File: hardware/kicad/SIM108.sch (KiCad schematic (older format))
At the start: 56 parts, among them J1 Screw_Terminal_01x09, J2 CAN, SW1 PRG, SW2 INSTANCE, SW3 BUS, U1 MCP2551-I-P, U2 TMR_2411, U3 74HCT595, U4 74HCT595, U5 Teensy_4.0

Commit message: Relay PCB
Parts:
- removed C1, C2, C3, C4: 100nF, Capacitor_SMD:C_0805_2012Metric, symbol Device:CP_Small
- removed C5: 100nF, Capacitor_THT:CP_Radial_D5.0mm_P2.50mm, symbol Device:CP_Small
- removed D1, D18, D19, D2, D20, D21, D22, D23, D24, D25, D3, D4, D5, D6, D7, D8, D9: LED, LED_THT:LED_D1.8mm_W3.3mm_H2.4mm, symbol Device:LED
- removed F1: 1A, Fuse:Fuse_Littelfuse_395Series, symbol Device:Polyfuse
- removed J2: CAN, Connector_PinHeader_2.54mm:PinHeader_1x05_P2.54mm_Vertical, symbol Connector:Screw_Terminal_01x05
- removed R1: 4K7 0.125W, Resistor_SMD:R_0805_2012Metric, symbol Device:R
- removed R2: 120R 0.5W, Resistor_THT:R_Axial_DIN0207_L6.3mm_D2.5mm_P7.62mm_Horizontal, symbol Device:R
- removed R28, R29, R3, R30, R31, R32, R33, R34, R35, R40, R41, R42, R43, R44, R45, R46, R47: 560R, Resistor_SMD:R_0805_2012Metric, symbol Device:R
- removed R36, R38: 2K2 0.125W, Resistor_SMD:R_0805_2012Metric, symbol Device:R
- removed R37, R39: 3K3 0.125W, Resistor_SMD:R_0805_2012Metric, symbol Device:R
- removed SW1: PRG, Button_Switch_THT:SW_TH_Tactile_Omron_B3F-10xx, symbol Switch:SW_MEC_5E
- removed SW2: INSTANCE, Package_DIP:DIP-16_W7.62mm, symbol Switch:SW_DIP_x08
- removed SW3: BUS, Package_DIP:DIP-4_W7.62mm_LongPads, symbol Switch:SW_DIP_x02
- removed U1: MCP2551-I-P, Package_SO:SOIC-8_3.9x4.9mm_P1.27mm, symbol Interface_CAN_LIN:MCP2551-I-P
- removed U2: TMR_2411, PDJR_DC-DC_Converters:TMR_2411, symbol SIM108-rescue:TMR_2411-pdjr
- removed U3, U4: 74HCT595, Package_SO:SO-16_3.9x9.9mm_P1.27mm, symbol 74xx:74HC595
- removed U5: Teensy_4.0, Package_DIP:DIP-28_W15.24mm_LongPads, symbol SIM108-rescue:Teensy_3.2-pdjr
- added D101, D102, D103, D104, D105, D106, D107, D108: IN4007, Diode_SMD:D_SOT-23_ANK, symbol Simulation_SPICE:DIODE
- added Q101, Q103, Q105, Q107, Q109, Q111, Q113, Q115: BC547, Package_TO_SOT_SMD:TSOT-23, symbol Transistor_BJT:BC547
- added Q102, Q104, Q106, Q108, Q110, Q112, Q114, Q116: BC337-40, Package_TO_SOT_SMD:TSOT-23, symbol Transistor_BJT:BC337
- added R101, R104, R107, R110, R113, R116, R119, R122: 4K7 0.125W, Resistor_SMD:R_0805_2012Metric, symbol Device:R
- added R102, R105, R108, R111, R114, R117, R120, R123: 10K 0.5W, Resistor_SMD:R_0805_2012Metric, symbol Device:R
- added R103, R106, R109, R112, R115, R118, R121, R124: 100R 0.25W, Resistor_SMD:R_0805_2012Metric, symbol Device:R
- added U101, U102, U103, U104, U105, U106, U107, U108: SFH617A-1, Package_DIP:SMDIP-4_W7.62mm, symbol Isolator:SFH617A-1
- renumbered J1 to J101
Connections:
- net labels added: +3.3V, D16, D17, D18, D19, D20, D21, D22, D23
- net labels removed: +5V, 3V3, ADDR_0, ADDR_1, ADDR_2, ADDR_3, ADDR_4, ADDR_5, ADDR_6, ADDR_7, CAN_H, CAN_L, CAN_RX, CAN_RX_3V3, CAN_SCR, CAN_TX, CAN_TX_3V3, CH0, CH1, CH2, CH3, CH4, CH5, CH6, CH7, MPX_CLOCK, MPX_DATA, MPX_LATCH, MPX_SER, PRG, SPST_CH0, SPST_CH1, SPST_CH2, SPST_CH3, SPST_CH4, SPST_CH5, SPST_CH6, SPST_CH7, TRANSMIT_LED
- wire segments 238 -> 184
- no-connect marks 9 -> 1
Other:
- note removed: "CAN_H"
- note removed: "CAN_L"
- note removed: "CAN_SCR"
- note removed: "CONFIGURATION"
- note removed: "DISPLAY"
- note removed: "NET_C"
- note removed: "NET_S"
- note removed: "Opto-isolated SPST inputs. Each opto-isolator\nis driven by a constant current source which\noperates the isolator LED at 6mA from voltages\nin the range 5VDC through 50VDC."
- note removed: "POWER SUPPLY & CAN INTERFACE"
- moved on the sheet: J101

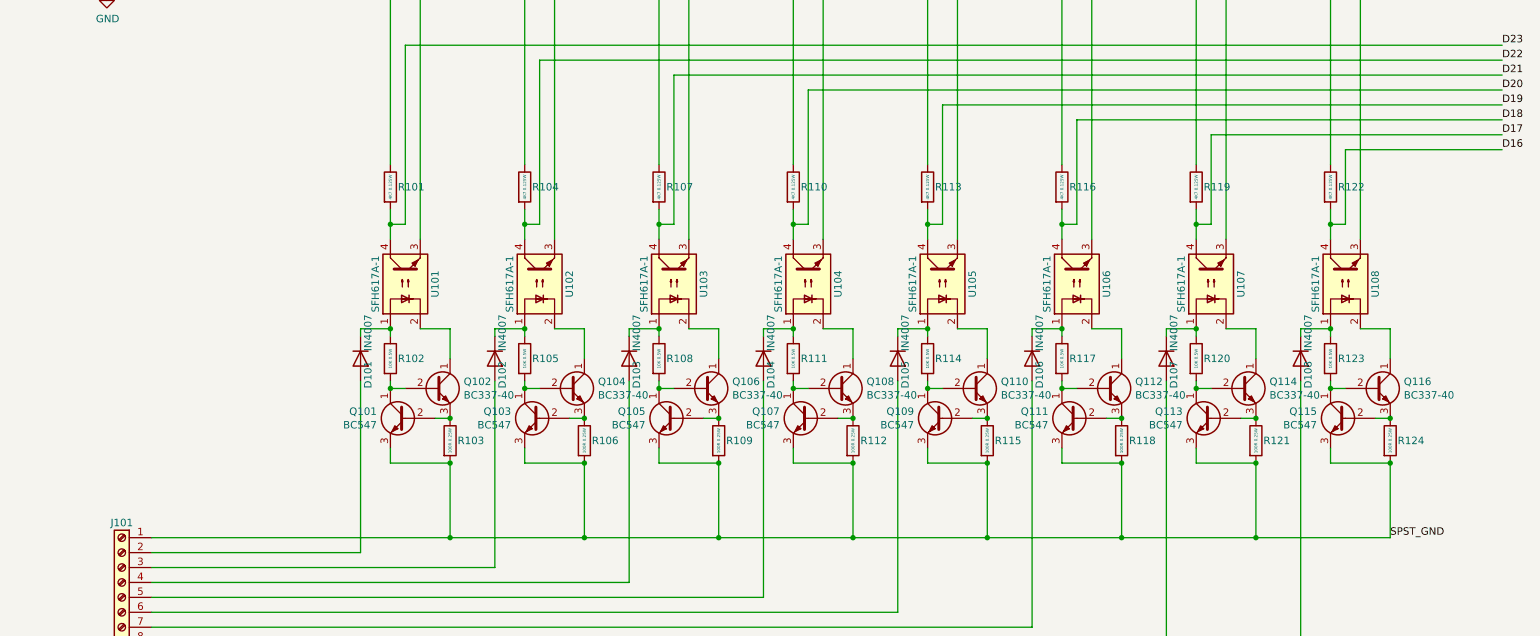
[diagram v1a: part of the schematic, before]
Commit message: Use new NOP100
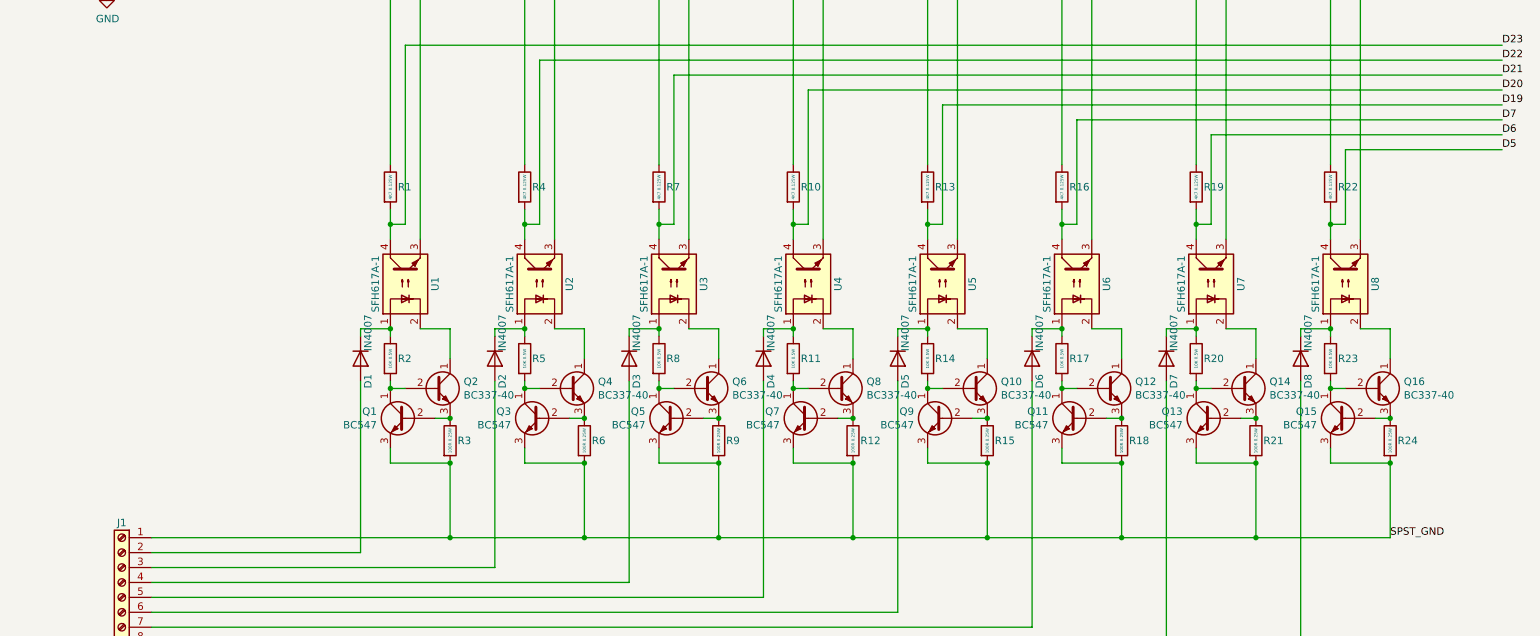
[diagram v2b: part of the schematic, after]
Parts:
- renumbered D101 to D1, D102 to D2, D103 to D3, D104 to D4, D105 to D5, D106 to D6, D107 to D7, D108 to D8, J101 to J1, Q101 to Q1, Q110 to Q10, Q111 to Q11, Q112 to Q12, Q113 to Q13, Q114 to Q14, Q115 to Q15, Q116 to Q16, Q102 to Q2, Q103 to Q3, Q104 to Q4, Q105 to Q5, Q106 to Q6, Q107 to Q7, Q108 to Q8, Q109 to Q9, R101 to R1, R110 to R10, R111 to R11, R112 to R12, R113 to R13, R114 to R14, R115 to R15, R116 to R16, R117 to R17, R118 to R18, R119 to R19, R102 to R2, R120 to R20, R121 to R21, R122 to R22, R123 to R23, R124 to R24, R103 to R3, R104 to R4, R105 to R5, R106 to R6, R107 to R7, R108 to R8, R109 to R9, U101 to U1, U102 to U2, U103 to U3, U104 to U4, U105 to U5, U106 to U6, U107 to U7, U108 to U8
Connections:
- net D16 renamed D5
- net D17 renamed D6
- net D18 renamed D7

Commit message: Relay PCB
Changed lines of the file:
@@
 	2500 3350 2700 3350
 Wire Wire Line
-	800  750  2700 750
+	800  750  1000 750
 Wire Wire Line
 	800  1100 2900 1100
@@
 Text Label 9400 4750 0    50   ~ 0
 SPST_GND
+$Comp
+L power:PWR_FLAG #FLG0101
+U 1 1 63AD42D9
+P 800 1100
+F 0 "#FLG0101" H 800 1175 50  0001 C CNN
+F 1 "PWR_FLAG" H 800 1273 50  0001 C CNN
+F 2 "" H 800 1100 50  0001 C CNN
+F 3 "~" H 800 1100 50  0001 C CNN
+	1    800  1100
+	1    0    0    -1
+$EndComp
+Connection ~ 1000 750
+Wire Wire Line
+	1000 750  2700 750
+$Comp
+L power:PWR_FLAG #FLG0102
+U 1 1 63AD4AFF
+P 800 750
+F 0 "#FLG0102" H 800 825 50  0001 C CNN
+F 1 "PWR_FLAG" H 800 923 50  0001 C CNN
+F 2 "" H 800 750 50  0001 C CNN
+F 3 "~" H 800 750 50  0001 C CNN
+	1    800  750
+	-1   0    0    1
+$EndComp
+Connection ~ 800  750
+Connection ~ 800  1100
 $EndSCHEMATC

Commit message: New PCB layout
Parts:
- removed D1, D2, D3, D4, D5, D6, D7, D8: IN4007, Diode_SMD:D_SOT-23_ANK, symbol Simulation_SPICE:DIODE
- removed J1: Screw_Terminal_01x09, PDJR_Connectors:CAMDEN_BOSS_CSTBV2-9_TERMINAL, symbol Connector:Screw_Terminal_01x09
- removed Q1, Q11, Q13, Q15, Q3, Q5, Q7, Q9: BC547, Package_TO_SOT_SMD:TSOT-23, symbol Transistor_BJT:BC547
- removed Q10, Q12, Q14, Q16, Q2, Q4, Q6, Q8: BC337-40, Package_TO_SOT_SMD:TSOT-23, symbol Transistor_BJT:BC337
- removed R1, R10, R13, R16, R19, R22, R4, R7: 4K7 0.125W, Resistor_SMD:R_0805_2012Metric, symbol Device:R
- removed R11, R14, R17, R2, R20, R23, R5, R8: 10K 0.5W, Resistor_SMD:R_0805_2012Metric, symbol Device:R
- removed R12, R15, R18, R21, R24, R3, R6, R9: 100R 0.25W, Resistor_SMD:R_0805_2012Metric, symbol Device:R
- removed U1, U2, U3, U4, U5, U6, U7, U8: SFH617A-1, Package_DIP:SMDIP-4_W7.62mm, symbol Isolator:SFH617A-1
- added C1, C10, C2, C3, C4, C5, C6, C7, C8, C9: CP1_Small, Capacitor_SMD:C_0504_1310Metric, symbol Device:CP1_Small
- added J1: Screw_Terminal_01x17, PDJR_Connectors:PHOENIX_SPTAF_3_5_17, symbol Connector:Screw_Terminal_01x17
- added RN1, RN2, RN3, RN4: R_Pack04, Resistor_SMD:R_Array_Convex_4x1206, symbol Device:R_Pack04
- added U1, U10, U11, U12, U13, U15, U16, U18, U19, U2, U21, U22, U4, U5, U7, U8: CL220K4-G, Package_TO_SOT_SMD:TO-252-2, symbol Driver_LED:CL220K4-G
- added U14, U20, U3, U9: ASCL-6400, Package_SO:SO-16_5.3x10.2mm_P1.27mm, symbol pdjr:ASCL-6400
- added U17, U6: 74LS165, Package_SO:SOP-16_4.4x10.4mm_P1.27mm, symbol pdjr:74LS165
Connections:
- net +3V3: now also C1.1, C10.1, C2.1, C3.1, C4.1, C5.1, C6.1, C7.1, C8.1, C9.1, RN1.5 (R4.2), RN1.6 (R3.2), RN1.7 (R2.2), RN1.8 (R1.2), RN2.5 (R4.2), RN2.6 (R3.2), RN2.7 (R2.2), RN2.8 (R1.2), RN3.5 (R4.2), RN3.6 (R3.2), RN3.7 (R2.2), RN3.8 (R1.2), RN4.5 (R4.2), RN4.6 (R3.2), RN4.7 (R2.2), RN4.8 (R1.2), U14.10 (VDD), U14.15 (VDD), U17.10 (DS), U17.15 (~CE), U17.16 (VCC), U20.10 (VDD), U20.15 (VDD), U3.10 (VDD), U3.15 (VDD), U6.10 (DS), U6.15 (~CE), U6.16 (VCC), U9.10 (VDD), U9.15 (VDD)
- net D21: now also U17.2 (CP), U6.2 (CP)
- net D22: now also U17.1 (~PL), U6.1 (~PL)
- net D23: now also U6.9 (Q7)
- net GND: now also C1.2, C10.2, C2.2, C3.2, C4.2, C5.2, C6.2, C7.2, C8.2, C9.2, U14.16 (GND), U14.9 (GND), U17.8 (GND), U20.16 (GND), U20.9 (GND), U3.16 (GND), U3.9 (GND), U6.8 (GND), U9.16 (GND), U9.9 (GND)
- new net: RN3.1 (R1.1), U14.11 (V4), U17.14 (D3)
- new net: RN3.2 (R2.1), U14.12 (V3), U17.13 (D2)
- new net: RN3.3 (R3.1), U14.13 (V2), U17.12 (D1)
- new net: RN3.4 (R4.1), U14.14 (V1), U17.11 (D0)
- new net: U2.1 (VA), U3.3 (A2)
- new net: J1.3 (Pin_3), U2.2 (VB)
- new net: U3.5 (A3), U4.1 (VA)
- new net: J1.4 (Pin_4), U4.2 (VB)
- new net: U3.7 (A4), U5.1 (VA)
- new net: J1.5 (Pin_5), U5.2 (VB)
- new net: U1.1 (VA), U3.1 (A1)
- new net: J1.2 (Pin_2), U1.2 (VB)
- new net: RN4.1 (R1.1), U17.6 (D7), U20.11 (V4)
- new net: RN4.2 (R2.1), U17.5 (D6), U20.12 (V3)
- new net: RN4.3 (R3.1), U17.4 (D5), U20.13 (V2)
- new net: RN4.4 (R4.1), U17.3 (D4), U20.14 (V1)
- new net: RN1.1 (R1.1), U3.11 (V4), U6.14 (D3)
- new net: RN1.2 (R2.1), U3.12 (V3), U6.13 (D2)
- new net: RN1.3 (R3.1), U3.13 (V2), U6.12 (D1)
- new net: RN1.4 (R4.1), U3.14 (V1), U6.11 (D0)
- new net: J1.1 (Pin_1), U14.2 (C1), U14.4 (C2), U14.6 (C3), U14.8 (C4), U20.2 (C1), U20.4 (C2), U20.6 (C3), U20.8 (C4), U3.2 (C1), U3.4 (C2), U3.6 (C3), U3.8 (C4), U9.2 (C1), U9.4 (C2), U9.6 (C3), U9.8 (C4)
- new net: U7.1 (VA), U9.1 (A1)
- new net: RN2.1 (R1.1), U6.6 (D7), U9.11 (V4)
- new net: RN2.2 (R2.1), U6.5 (D6), U9.12 (V3)
- new net: RN2.3 (R3.1), U6.4 (D5), U9.13 (V2)
- new net: RN2.4 (R4.1), U6.3 (D4), U9.14 (V1)
- new net: U8.1 (VA), U9.3 (A2)
- new net: U10.1 (VA), U9.5 (A3)
- new net: U11.1 (VA), U9.7 (A4)
- new net: U17.9 (Q7), U6.7 (~Q7)
- new net: J1.7 (Pin_7), U8.2 (VB)
- new net: J1.8 (Pin_8), U10.2 (VB)
- new net: J1.9 (Pin_9), U11.2 (VB)
- new net: J1.6 (Pin_6), U7.2 (VB)
- new net: U12.1 (VA), U14.1 (A1)
- new net: U13.1 (VA), U14.3 (A2)
- new net: U14.5 (A3), U15.1 (VA)
- new net: U14.7 (A4), U16.1 (VA)
- new net: U18.1 (VA), U20.1 (A1)
- new net: U19.1 (VA), U20.3 (A2)
- new net: U20.5 (A3), U21.1 (VA)
- new net: U20.7 (A4), U22.1 (VA)
- new net: J1.11 (Pin_11), U13.2 (VB)
- new net: J1.12 (Pin_12), U15.2 (VB)
- new net: J1.13 (Pin_13), U16.2 (VB)
- new net: J1.10 (Pin_10), U12.2 (VB)
- new net: J1.15 (Pin_15), U19.2 (VB)
- new net: J1.16 (Pin_16), U21.2 (VB)
- new net: J1.17 (Pin_17), U22.2 (VB)
- new net: J1.14 (Pin_14), U18.2 (VB)

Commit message: Gerber order
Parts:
- removed J1: Screw_Terminal_01x17, PDJR_Connectors:PHOENIX_SPTAF_3_5_17, symbol Connector:Screw_Terminal_01x17
- removed U1, U10, U11, U12, U13, U15, U16, U18, U19, U2, U21, U22, U4, U5, U7, U8: CL220K4-G, Package_TO_SOT_SMD:TO-252-2, symbol Driver_LED:CL220K4-G
- added D1, D10, D11, D12, D13, D14, D15, D16, D2, D3, D4, D5, D6, D7, D8, D9: D_Small, Diode_SMD:D_0805_2012Metric, symbol Device:D_Small
- added J1, J2: Screw_Terminal_01x09, PDJR_Connectors:897-1357-9-PIN-3-5-CONN, symbol Connector:Screw_Terminal_01x09
- added U1, U2, U4: BCR401, PDJR_Connectors:BCR401, symbol SIM108-rescue:BCR401-pdjr
- added U10, U11, U12, U13, U15, U16, U18, U19, U21, U22, U5, U7, U8: BCR401 (16x), PDJR_Connectors:BCR401, symbol SIM108-rescue:BCR401-pdjr
- C1, C10, C2, C3, C4, C5, C6, C7, C8, C9: value CP1_Small -> 100nF
- RN1, RN2, RN3, RN4: value R_Pack04 -> 4K
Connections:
- net +3V3: no longer U17.10 (DS), U17.15 (~CE), U6.10 (DS), U6.15 (~CE)
- net GND: now also U17.10 (DS), U17.15 (~CE), U6.15 (~CE)
- net at U3.3 (A2): now also U2.2 (OUT), U2.3 (OUT), U2.5 (OUT)
- net at U3.5 (A3): now also U4.2 (OUT), U4.3 (OUT), U4.5 (OUT)
- net at U3.7 (A4): now also U5.2 (OUT), U5.3 (OUT), U5.5 (OUT)
- net at U3.1 (A1): now also U1.2 (OUT), U1.3 (OUT), U1.5 (OUT)
- net at U14.2 (C1), U14.4 (C2), U14.6 (C3)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: now also J1.1 (Pin_1), J2.9 (Pin_9), U1.1 (GND), U10.1 (GND), U11.1 (GND), U12.1 (GND), U13.1 (GND), U15.1 (GND), U16.1 (GND), U18.1 (GND), U19.1 (GND), U2.1 (GND), U21.1 (GND), U22.1 (GND), U4.1 (GND), U5.1 (GND), U7.1 (GND), U8.1 (GND)
- net at U9.1 (A1): now also U7.2 (OUT), U7.3 (OUT), U7.5 (OUT)
- net at U9.3 (A2): now also U8.2 (OUT), U8.3 (OUT), U8.5 (OUT)
- net at U9.5 (A3): now also U10.2 (OUT), U10.3 (OUT), U10.5 (OUT)
- net at U9.7 (A4): now also U11.2 (OUT), U11.3 (OUT), U11.5 (OUT)
- net at U17.9 (Q7): now also U6.10 (DS); no longer U6.7 (~Q7)
- net at U14.1 (A1): now also U12.2 (OUT), U12.3 (OUT), U12.5 (OUT)
- net at U14.3 (A2): now also U13.2 (OUT), U13.3 (OUT), U13.5 (OUT)
- net at U14.5 (A3): now also U15.2 (OUT), U15.3 (OUT), U15.5 (OUT)
- net at U14.7 (A4): now also U16.2 (OUT), U16.3 (OUT), U16.5 (OUT)
- net at U20.1 (A1): now also U18.2 (OUT), U18.3 (OUT), U18.5 (OUT)
- net at U20.3 (A2): now also U19.2 (OUT), U19.3 (OUT), U19.5 (OUT)
- net at U20.5 (A3): now also U21.2 (OUT), U21.3 (OUT), U21.5 (OUT)
- net at U20.7 (A4): now also U22.2 (OUT), U22.3 (OUT), U22.5 (OUT)
- net D21 renamed D17
- net D22 renamed D16
- new net: D1.1 (K), U1.4 (Vs)
- new net: D1.2 (A), J1.2 (Pin_2)
- new net: D2.1 (K), U2.4 (Vs)
- new net: D2.2 (A), J1.3 (Pin_3)
- new net: D3.1 (K), U4.4 (Vs)
- new net: D3.2 (A), J1.4 (Pin_4)
- new net: D4.1 (K), U5.4 (Vs)
- new net: D4.2 (A), J1.5 (Pin_5)
- new net: D5.1 (K), U7.4 (Vs)
- new net: D5.2 (A), J1.6 (Pin_6)
- new net: D6.1 (K), U8.4 (Vs)
- new net: D6.2 (A), J1.7 (Pin_7)
- new net: D7.1 (K), U10.4 (Vs)
- new net: D7.2 (A), J1.8 (Pin_8)
- new net: D8.1 (K), U11.4 (Vs)
- new net: D8.2 (A), J1.9 (Pin_9)
- new net: D9.1 (K), U12.4 (Vs)
- new net: D9.2 (A), J2.1 (Pin_1)
- new net: D10.1 (K), U13.4 (Vs)
- new net: D10.2 (A), J2.2 (Pin_2)
- new net: D11.1 (K), U15.4 (Vs)
- new net: D11.2 (A), J2.3 (Pin_3)
- new net: D12.1 (K), U16.4 (Vs)
- new net: D12.2 (A), J2.4 (Pin_4)
- new net: D13.1 (K), U18.4 (Vs)
- new net: D13.2 (A), J2.5 (Pin_5)
- new net: D14.1 (K), U19.4 (Vs)
- new net: D14.2 (A), J2.6 (Pin_6)
- new net: D15.1 (K), U21.4 (Vs)
- new net: D15.2 (A), J2.7 (Pin_7)
- new net: D16.1 (K), U22.4 (Vs)
- new net: D16.2 (A), J2.8 (Pin_8)
- no-connect marks 1 -> 3
